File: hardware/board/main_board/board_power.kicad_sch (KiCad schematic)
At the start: 31 parts, among them J6 Barrel_Jack_Switch, U11 LM27762, U16 rt6150b-33gqw, U19 MCP16312x-xMNY

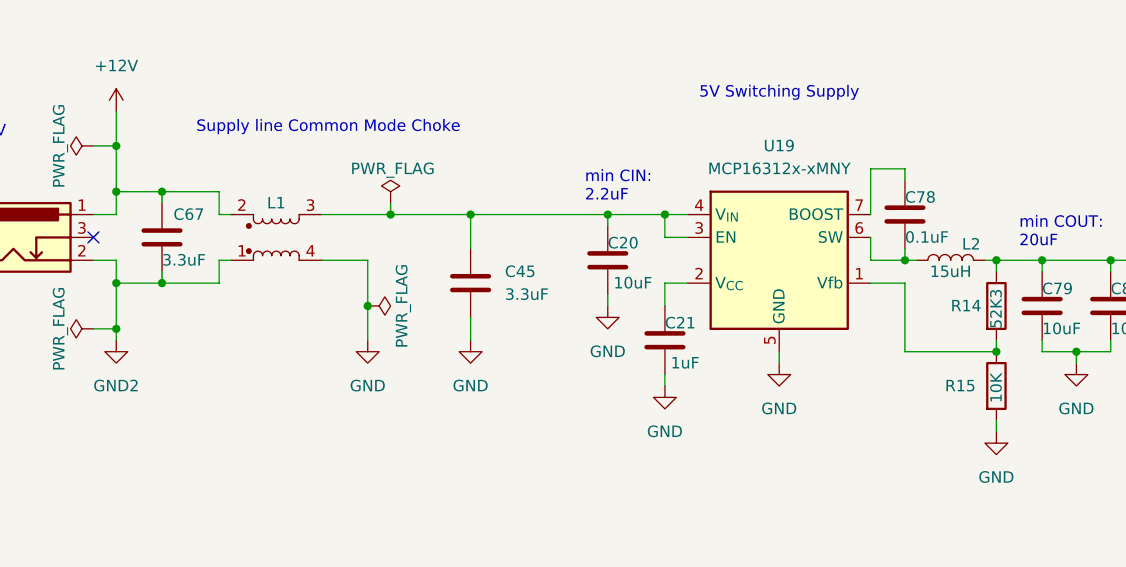
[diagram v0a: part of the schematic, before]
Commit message: update buffer board soldermask cutout
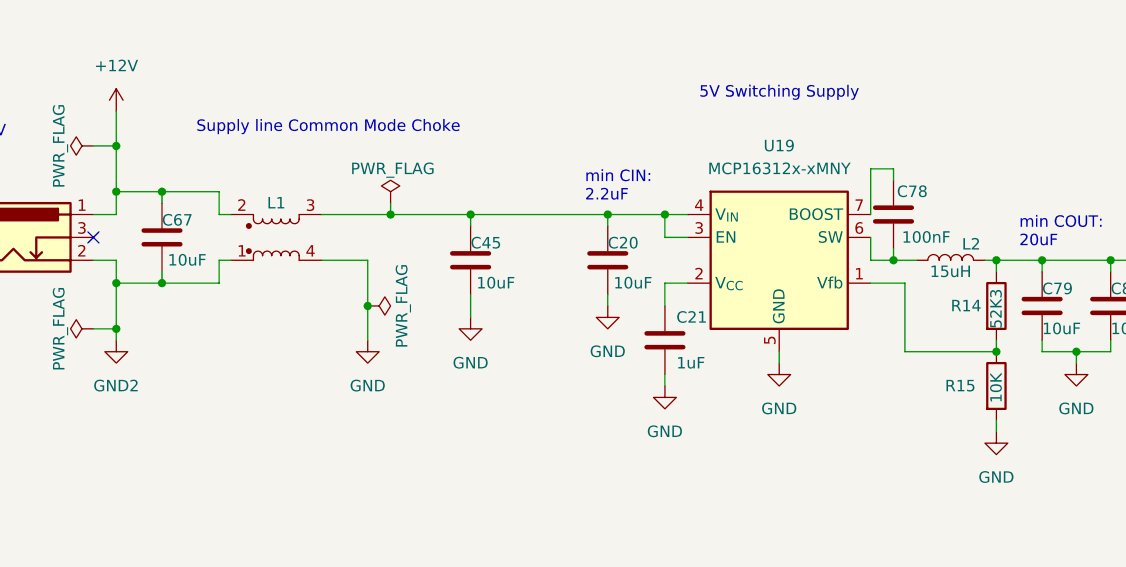
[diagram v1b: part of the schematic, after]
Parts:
- C20, C79, C80: Link https://www.digikey.com/en/products/detail/cal-chip-electro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 -> https://www.digikey.com/en/products/detail/murata-electroni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; Manufacturer Cal-Chip Electronics, Inc. -> Murata Electronics; Manufacturer Number GMC21X7R106K25NT -> GRM21BZ71E106KE15L; Rated Voltage (none) -> 25V
- C21: footprint Capacitor_SMD:C_0805_2012Metric -> Capacitor_SMD:C_0402_1005Metric; Link https://www.digikey.com/en/products/detail/tdk-corporation/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 -> https://www.digikey.com/en/products/detail/murata-electroni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; Manufacturer TDK Corporation -> Murata Electronics; Manufacturer Number C2012X7R1H105K125AB -> GRM155R6YA105KE11J; Rated Voltage (none) -> 35V; Temperature Coefficient (none) -> X5R
- C45, C67: value 3.3uF -> 10uF; Link https://www.digikey.com/en/products/detail/tdk-corporation/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 -> https://www.digikey.com/en/products/detail/murata-electroni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; Manufacturer TDK Corporation -> Murata Electronics; Manufacturer Number CGA4J1X7R1E335K125AC -> GRM21BZ71E106KE15L; Temperature Coefficient X7R -> (none); Tolerance 10% -> (none)
- C76, C77: Alternate CL21B106KOQNNNE -> (none)
- C78: value 0.1uF -> 100nF; footprint Capacitor_SMD:C_0603_1608Metric -> Capacitor_SMD:C_0402_1005Metric; Link https://www.digikey.com/en/products/detail/tdk-corporation/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 -> https://www.digikey.com/en/products/detail/walsin-technolog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; Manufacturer TDK Corporation -> Walson Technology Corporation; Manufacturer Number CGA3E2X7R1H104K080AA -> 0402B104K160CT; PCBWay Link (none) -> https://www.pcbway.com/components/detail/0402B104K160CT/307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; Rated Voltage (none) -> 16V; Temperature Coefficient (none) -> X7R; Tolerance (none) -> 10%
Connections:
- net at L2.1, U19.6 (SW): now also C78.1; no longer C78.2
- net at U19.7 (BOOST): now also C78.2; no longer C78.1

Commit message: add split pcba design
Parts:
- R59, R76: Link https://www.digikey.com/en/products/detail/yageo/RC0402FR-0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 -> https://www.digikey.com/en/products/detail/yageo/RT0402BRD0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; Manufacturer Number RC0402FR-07100KL -> RT0402BRD07100KL; Tolerance 1% -> 0.1%
- U19: Link (none) -> https://www.digikey.com/en/products/detail/microchip-techno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
